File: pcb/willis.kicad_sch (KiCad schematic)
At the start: 112 parts, among them J1 SWD, J2 Battery, J3 USB-C Conn, J4 Battery JST, J5 TC2030_SWD, K1 KEYSW, K10 KEYSW, K11 KEYSW, K12 KEYSW, K13 KEYSW, K14 KEYSW, K15 KEYSW, K16 KEYSW, K17 KEYSW, K18 KEYSW, K19 KEYSW, K2 KEYSW, K20 KEYSW, K21 KEYSW, K22 KEYSW, K23 KEYSW, K24 KEYSW, K25 KEYSW, K26 KEYSW, K27 KEYSW, K28 KEYSW, K29 KEYSW, K3 KEYSW, K30 KEYSW, K31 KEYSW, K32 KEYSW, K33 KEYSW, K34 KEYSW, K35 KEYSW, K36 KEYSW, K37 KEYSW, K38 KEYSW, K4 KEYSW, K5 KEYSW, K6 KEYSW, K7 KEYSW, K8 KEYSW, K9 KEYSW, Q1 AO3407, U1 TP4054, U2 USBLC6-2SC6, U3 E73-2G4M08S1C-52840, X1 32.768kHz

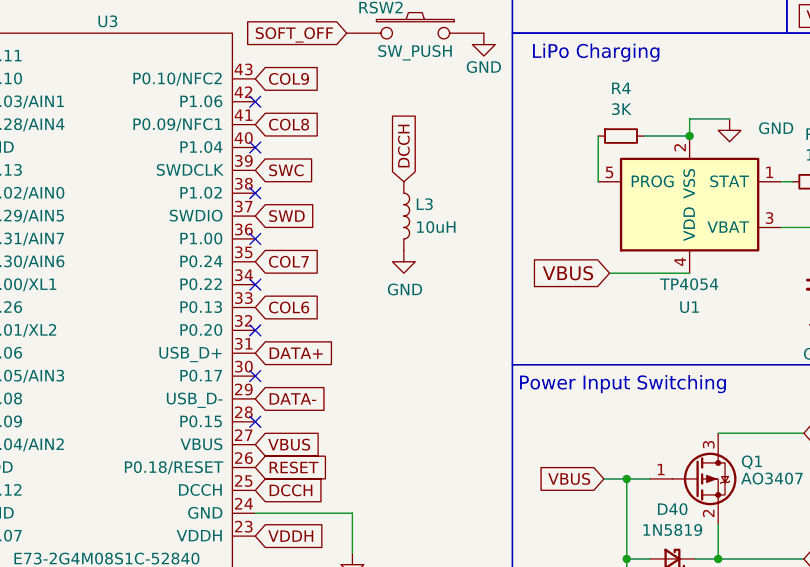
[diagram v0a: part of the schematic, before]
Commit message: V0.3: fixes for DCCH inductor circuit
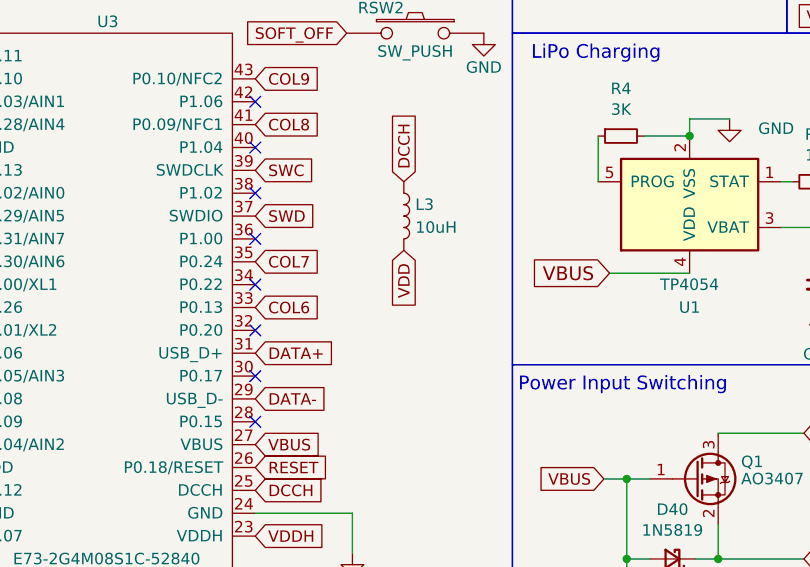
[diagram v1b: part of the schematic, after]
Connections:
- net GND: no longer L3.2
- net VDD: now also L3.2
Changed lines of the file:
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@@
 	(title_block
 		(title "Willis")
-		(date "2024-10-11")
-		(rev "V0.2")
+		(date "2024-11-16")
+		(rev "V0.3")
 		(company "krikun98")
 	)
@@
 		)
 	)
+	(global_label "VDD"
+		(shape input)
+		(at 77.47 152.4 270)
+		(fields_autoplaced yes)
+		(effects
+			(font
+				(size 1.27 1.27)
+			)
+			(justify right)
+		)
+		(property "Intersheetrefs" "${INTERSHEET_REFS}"
+			(at 77.47 159.0138 90)
+			(effects
+				(font
+					(size 1.27 1.27)
+				)
+				(justify right)
+				(hide yes)
+			)
+		)
+	)
 	(global_label "VBAT"
 		(shape input)
@@
 					(unit 1)
 				)
-			)
-		)
-	)
-	(symbol
-		(lib_id "power:GND")
-		(at 77.47 152.4 0)
-		(unit 1)
-		(exclude_from_sim no)
-		(in_bom yes)
-		(on_board yes)
-		(dnp no)
-		(property "Reference" "#PWR012"
-			(at 77.47 158.75 0)
-			(effects
-				(font
-					(size 1.27 1.27)
-				)
-				(hide yes)
-			)
-		)
-		(property "Value" "GND"
-			(at 77.597 156.7942 0)
-			(effects
-				(font
-					(size 1.27 1.27)
-				)
-			)
-		)
-		(property "Footprint" ""
-			(at 77.47 152.4 0)
-			(effects
-				(font
-					(size 1.27 1.27)
-				)
-				(hide yes)
-			)
-		)
-		(property "Datasheet" ""
-			(at 77.47 152.4 0)
-			(effects
-				(font
-					(size 1.27 1.27)
-				)
-				(hide yes)
-			)
-		)
-		(property "Description" ""
-			(at 77.47 152.4 0)
-			(effects
-				(font
-					(size 1.27 1.27)
-				)
-				(hide yes)
-			)
-		)
-		(pin "1"
-		)
-		(instances
-			(project "willis"
-				(path "/d115f25c-1917-4dd2-921b-1a223dfb969b"
-					(reference "#PWR012")
-					(unit 1)
-				)
